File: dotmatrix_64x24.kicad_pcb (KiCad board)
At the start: 2 copper layers, 180 x 100 mm, 597 parts, among them CON1 BARREL_JACK, P1 CONN_01X09, P2 CONN_01X09, P3 CONN_01X04, P4 CONN_01X03, P5 USB_OTG, P6 CONN_01X03, Q1 NJL7302L-F3, Q2 Q_PNP_BEC 2SA1162, Q3 Q_NPN_BCE RN5006, SW1 SW_PUSH_SMALL_H, SW2 SW_PUSH_SMALL_H, SW3 SW_PUSH_SMALL_H, SW4 SW_PUSH_SMALL_H, SW5 SW_PUSH_SMALL_H, SW6 SW_PUSH_SMALL_H, SW7 SW_PUSH_SMALL_H, SW8 SW_PUSH_SMALL_H, U1 WROOM-02, U10 LED1642GW, U11 LED1642GW, U12 AE-BME280, U13 OKL-T/6-W5, U14 NJU7223, U15 DS1307, U16 CH340G, U17 OSRB38C9AA, U18 BME280, U2 74HC595-alt-vdd, U3 TD62783, U4 74HC595-alt-vdd, U5 TD62783, U6 LED1642GW, U7 74HC595-alt-vdd, U8 TD62783, U9 LED1642GW, X1 CRYSTAL_SMD, Y1 12MHz

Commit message: Various fix and improvements
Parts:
- added C35: 1u, Capacitors_SMD:C_0603_HandSoldering, F.Cu at (22.3, 108.3)
- added REF**: stitch-via-0.6mm, components:stitch-via-0.6mm, F.Cu at (68.4, 99.7)
- added REF**: stitch-via-0.6mm, components:stitch-via-0.6mm, F.Cu at (16.7, 103.5)
- added REF**: stitch-via-0.6mm, components:stitch-via-0.6mm, F.Cu at (20.4, 105.9)
- added REF**: stitch-via-0.6mm, components:stitch-via-0.6mm, F.Cu at (19.3, 105.1)
- added REF**: stitch-via-0.6mm, components:stitch-via-0.6mm, F.Cu at (137.9, 78.0)
- added REF**: stitch-via-0.6mm, components:stitch-via-0.6mm, F.Cu at (93.8, 84.6)
- added REF**: stitch-via-0.6mm, components:stitch-via-0.6mm, F.Cu at (101.5, 91.3)
- added REF**: stitch-via-0.6mm, components:stitch-via-0.6mm, F.Cu at (105.2, 91.1)
- added REF**: stitch-via-0.6mm, components:stitch-via-0.6mm, F.Cu at (105.4, 93.6)
- added REF**: stitch-via-0.6mm, components:stitch-via-0.6mm, F.Cu at (90.9, 88.5)
- added REF**: stitch-via-0.6mm, components:stitch-via-0.6mm, F.Cu at (102.9, 87.9)
- added REF**: stitch-via-0.6mm, components:stitch-via-0.6mm, F.Cu at (69.4, 102.4)
- added REF**: stitch-via-0.6mm, components:stitch-via-0.6mm, F.Cu at (110.8, 77.4)
- added REF**: stitch-via-0.6mm, components:stitch-via-0.6mm, F.Cu at (132.2, 95.4)
- added REF**: stitch-via-0.6mm, components:stitch-via-0.6mm, F.Cu at (134.0, 104.5)
- added REF**: stitch-via-0.6mm, components:stitch-via-0.6mm, F.Cu at (129.9, 105.6)
- added REF**: stitch-via-0.6mm, components:stitch-via-0.6mm, F.Cu at (131.7, 102.2)
- added REF**: stitch-via-0.6mm, components:stitch-via-0.6mm, F.Cu at (115.0, 96.2)
- added REF**: stitch-via-0.6mm, components:stitch-via-0.6mm, F.Cu at (107.6, 91.9)
- added REF**: stitch-via-0.6mm, components:stitch-via-0.6mm, F.Cu at (109.6, 97.8)
- added REF**: stitch-via-0.6mm, components:stitch-via-0.6mm, F.Cu at (104.7, 99.3)
- added REF**: stitch-via-0.6mm, components:stitch-via-0.6mm, F.Cu at (106.3, 104.0)
- added REF**: stitch-via-0.6mm, components:stitch-via-0.6mm, F.Cu at (66.9, 102.5)
- added REF**: stitch-via-0.6mm, components:stitch-via-0.6mm, F.Cu at (112.9, 104.7)
- added REF**: stitch-via-0.6mm, components:stitch-via-0.6mm, F.Cu at (61.6, 104.1)
- added REF**: stitch-via-0.6mm, components:stitch-via-0.6mm, F.Cu at (44.8, 101.6)
- added REF**: stitch-via-0.6mm, components:stitch-via-0.6mm, F.Cu at (20.7, 107.3)
- added REF**: stitch-via-0.6mm, components:stitch-via-0.6mm, F.Cu at (23.6, 109.4)
- added REF**: stitch-via-0.6mm, components:stitch-via-0.6mm, F.Cu at (22.4, 110.9)
- added REF**: stitch-via-0.6mm, components:stitch-via-0.6mm, F.Cu at (20.7, 109.1)
- moved REF** 4.28 mm to (15.4, 103.5)
- moved REF** 2.46 mm to (182.7, 105.3)
- moved REF** 2.22 mm to (84.5, 78.3)
- moved REF** 2.18 mm to (106.7, 94.7)
- moved REF** 2.00 mm to (102.6, 100.4)
- moved REF** 1.65 mm to (57.5, 104.4)
- moved REF** 1.60 mm to (131.1, 78.1)
- moved REF** 1.16 mm to (20.1, 103.6)
- moved REF** 1.05 mm to (130.0, 95.4)
- moved JP7 0.66 mm to (183.8, 85.4)
- moved REF** 0.39 mm to (181.4, 86.8)
- moved REF** 0.23 mm to (109.8, 100.0)
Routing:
- net GND: track 1029.2 -> 1016.7 mm
- net VCC: track 570.9 -> 574.6 mm
- net /ESPVDD: track 210.1 -> 213.2 mm
- net Net-(JP7-Pad2): track 4.93 -> 6.00 mm

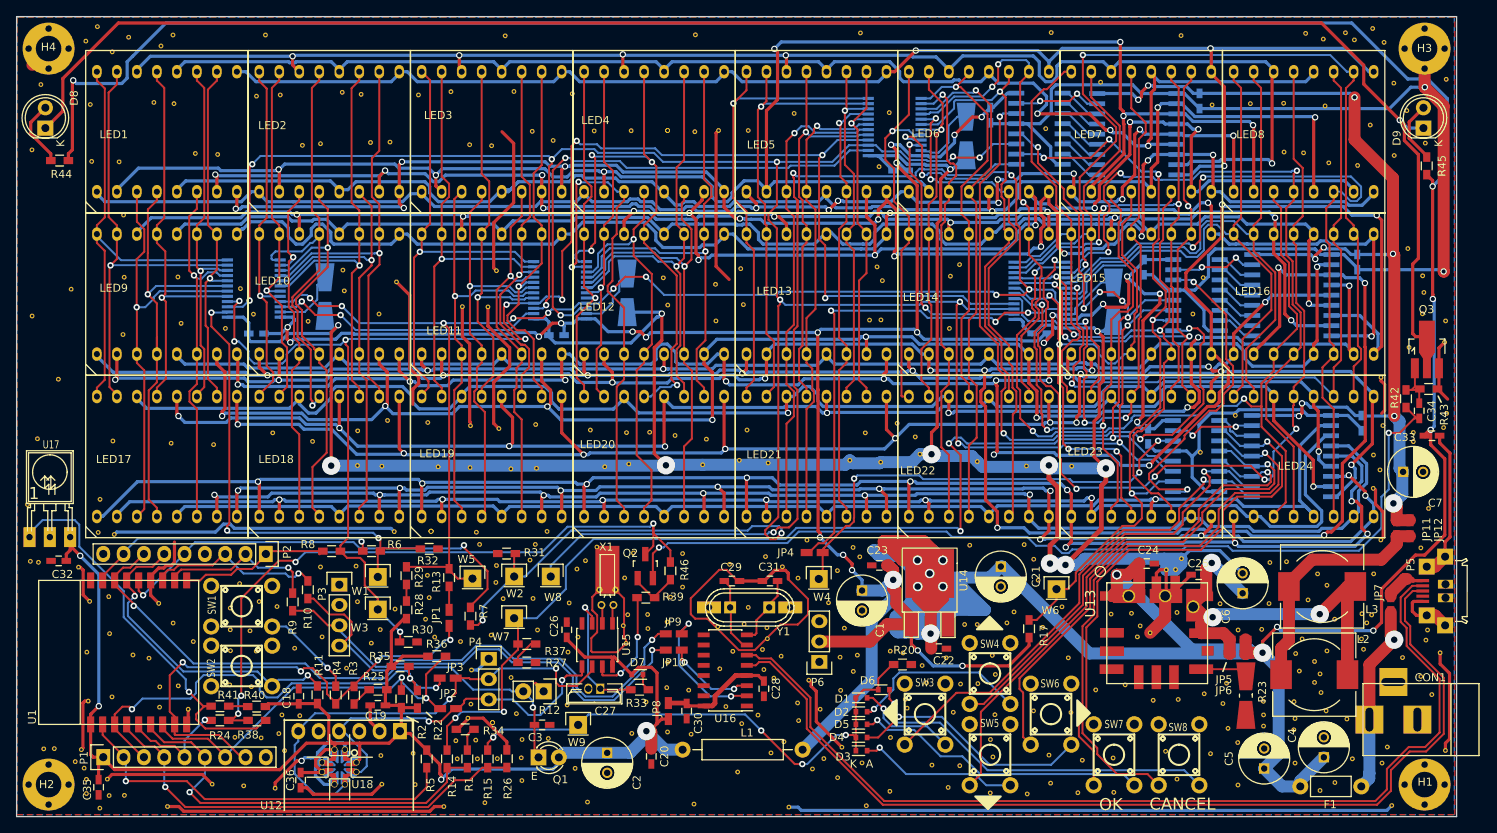
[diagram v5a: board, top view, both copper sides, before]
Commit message: Fixed current flow, cut antenna area of the PCB
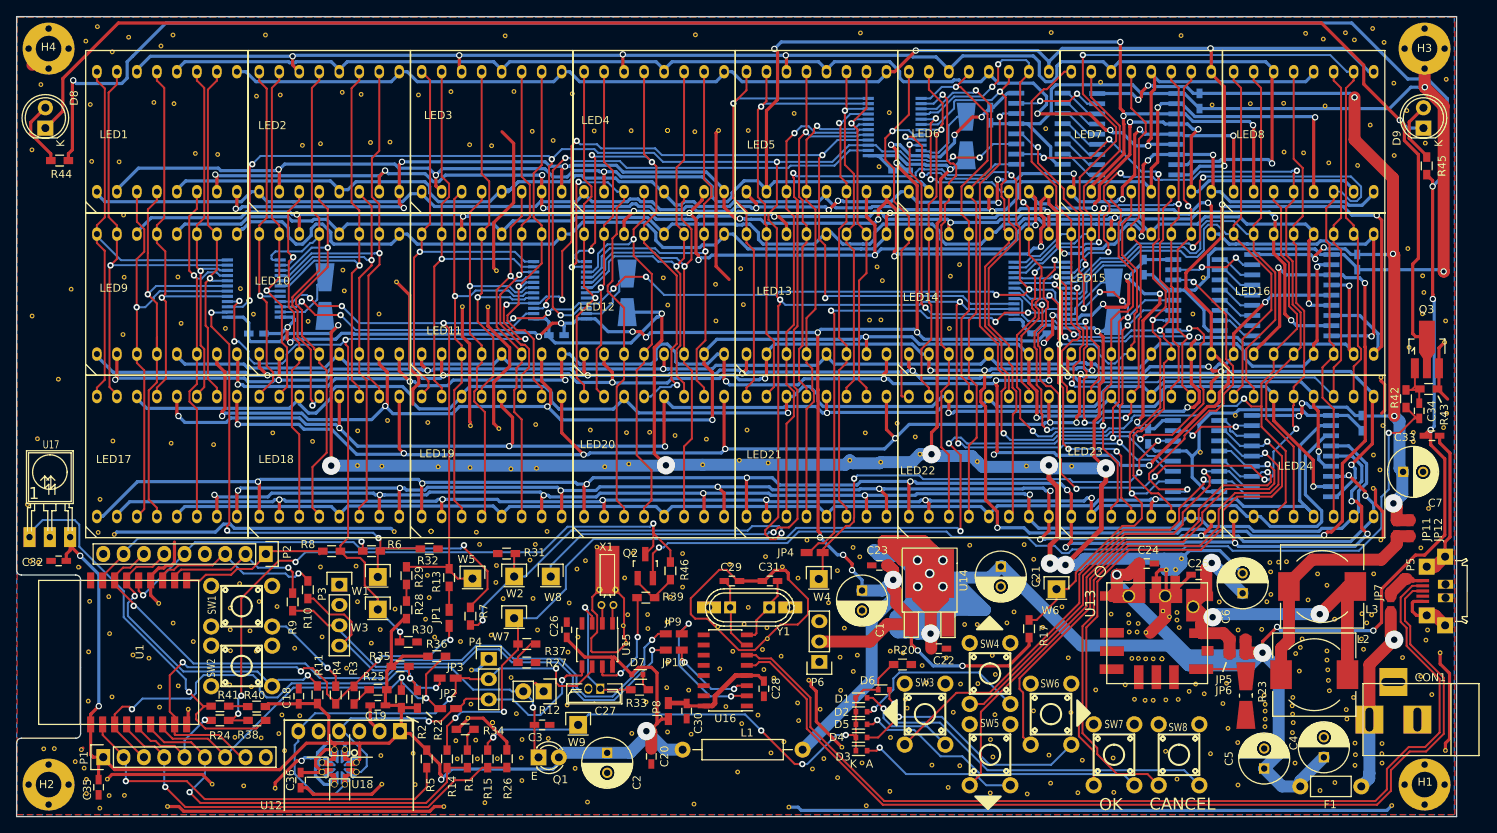
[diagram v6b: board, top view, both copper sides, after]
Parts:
- removed the REF** at (152.1, 89.5)
- added REF**: stitch-via-0.6mm, components:stitch-via-0.6mm, F.Cu at (168.8, 84.2)
- added REF**: stitch-via-0.6mm, components:stitch-via-0.6mm, F.Cu at (171.5, 101.5)
- added REF**: stitch-via-0.6mm, components:stitch-via-0.6mm, F.Cu at (171.4, 98.1)
- added REF**: stitch-via-0.6mm, components:stitch-via-0.6mm, F.Cu at (168.1, 98.0)
- added REF**: stitch-via-0.6mm, components:stitch-via-0.6mm, F.Cu at (159.4, 95.4)
- added REF**: stitch-via-0.6mm, components:stitch-via-0.6mm, F.Cu at (158.6, 96.3)
- added REF**: stitch-via-0.6mm, components:stitch-via-0.6mm, F.Cu at (155.7, 97.4)
- added REF**: stitch-via-0.6mm, components:stitch-via-0.6mm, F.Cu at (151.7, 97.3)
- added REF**: stitch-via-0.6mm, components:stitch-via-0.6mm, F.Cu at (153.1, 97.5)
- added REF**: stitch-via-0.6mm, components:stitch-via-0.6mm, F.Cu at (155.3, 86.3)
- added REF**: stitch-via-0.6mm, components:stitch-via-0.6mm, F.Cu at (156.1, 87.0)
- added REF**: stitch-via-0.6mm, components:stitch-via-0.6mm, F.Cu at (169.7, 80.2)
- added REF**: stitch-via-0.6mm, components:stitch-via-0.6mm, F.Cu at (157.3, 88.4)
- added REF**: stitch-via-0.6mm, components:stitch-via-0.6mm, F.Cu at (157.0, 87.4)
- added REF** (x2): stitch-via-0.6mm, components:stitch-via-0.6mm, F.Cu at (155.2, 92.3)
- added REF**: stitch-via-0.6mm, components:stitch-via-0.6mm, F.Cu at (154.1, 92.3)
- added REF**: stitch-via-0.6mm, components:stitch-via-0.6mm, F.Cu at (153.1, 92.3)
- added REF**: stitch-via-0.6mm, components:stitch-via-0.6mm, F.Cu at (152.2, 92.2)
- added REF**: stitch-via-0.6mm, components:stitch-via-0.6mm, F.Cu at (151.4, 92.2)
- added REF**: stitch-via-0.6mm, components:stitch-via-0.6mm, F.Cu at (151.0, 87.8)
- added REF**: stitch-via-0.6mm, components:stitch-via-0.6mm, F.Cu at (151.1, 88.9)
- added REF**: stitch-via-0.6mm, components:stitch-via-0.6mm, F.Cu at (168.8, 81.4)
- added REF**: stitch-via-0.6mm, components:stitch-via-0.6mm, F.Cu at (152.1, 88.9)
- added REF**: stitch-via-0.6mm, components:stitch-via-0.6mm, F.Cu at (179.3, 105.6)
- added REF**: stitch-via-0.6mm, components:stitch-via-0.6mm, F.Cu at (179.3, 104.3)
- added REF**: stitch-via-0.6mm, components:stitch-via-0.6mm, F.Cu at (182.7, 104.1)
- added REF**: stitch-via-0.6mm, components:stitch-via-0.6mm, F.Cu at (178.2, 98.6)
- added REF**: stitch-via-0.6mm, components:stitch-via-0.6mm, F.Cu at (172.5, 90.9)
- added REF**: stitch-via-0.6mm, components:stitch-via-0.6mm, F.Cu at (168.0, 100.8)
- moved REF** 3.82 mm to (179.1, 97.1)
- moved REF** 1.98 mm to (179.3, 102.8)
- moved REF** 1.75 mm to (176.0, 95.0)
- moved REF** 1.56 mm to (175.8, 92.4)
- moved REF** 1.09 mm to (175.9, 93.6)
- moved REF** 1.07 mm to (176.1, 96.3)
- moved REF** 0.89 mm to (171.6, 100.3)
- moved REF** 0.89 mm to (168.1, 99.8)
- moved REF** 0.79 mm to (182.7, 102.9)
- moved REF** 0.74 mm to (167.9, 96.9)
- moved REF** 0.64 mm to (171.5, 99.2)
- moved REF** 0.55 mm to (171.5, 97.1)
- moved REF** 0.54 mm to (153.2, 89.0)
- moved REF** 0.52 mm to (168.1, 98.8)
- moved REF** 0.40 mm to (152.2, 87.9)
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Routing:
- net GND: track 1016.7 -> 1005.6 mm
- net VCC: track 574.6 -> 569.9 mm
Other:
- outline, holes or cut-outs redrawn

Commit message: Various fixes, notably removing front coppor pour under Murata DC-DC converter
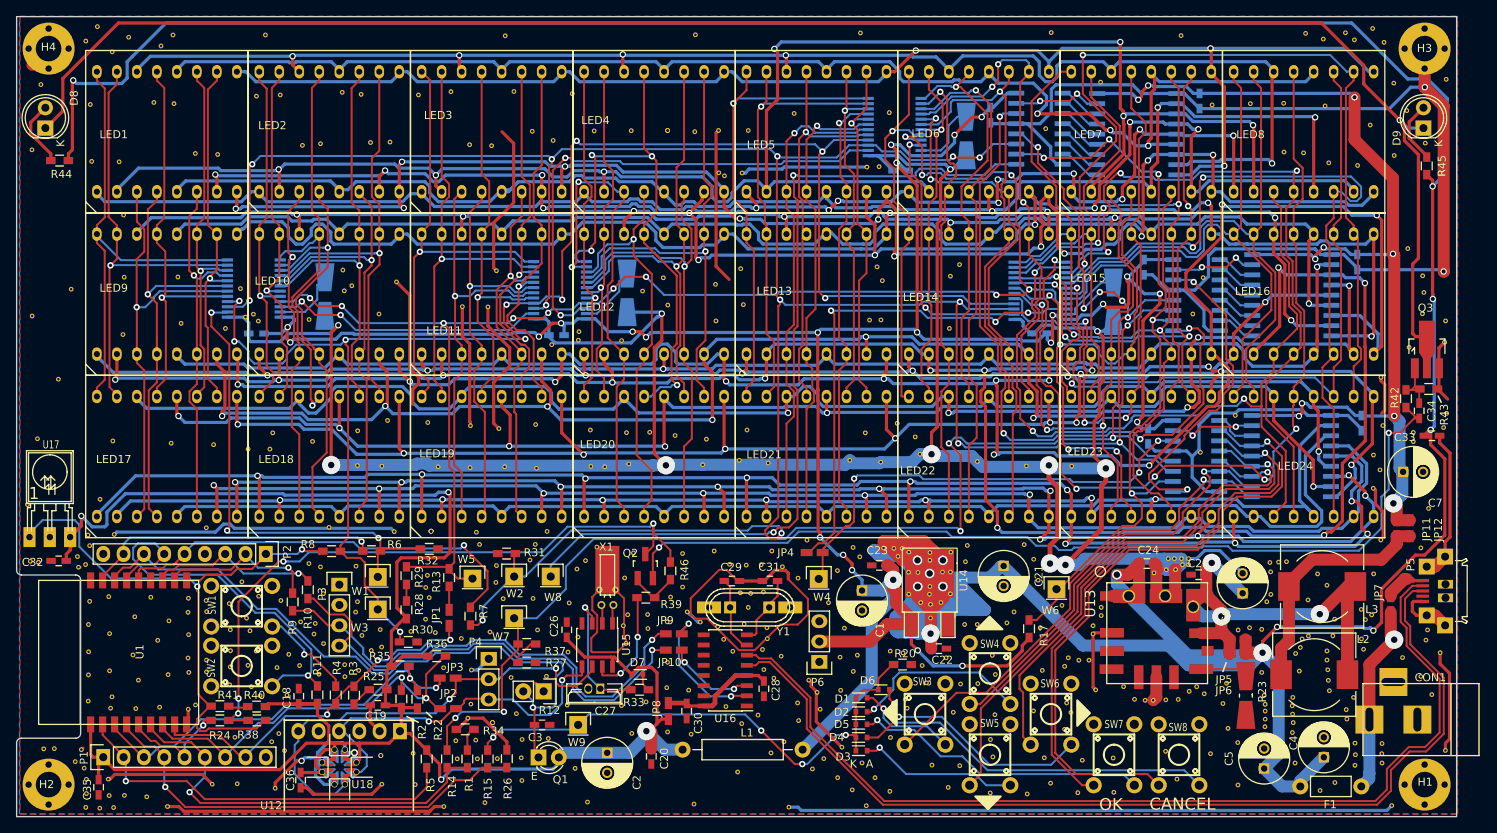
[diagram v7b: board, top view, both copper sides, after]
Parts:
- removed the REF** at (152.2, 87.9)
- removed the REF** at (162.3, 85.2)
- removed the REF** at (40.4, 108.2)
- removed the REF** at (155.3, 86.3)
- removed the REF** at (44.6, 85.8)
- removed the REF** at (156.1, 87.0)
- removed the REF** at (157.3, 88.4)
- removed the REF** at (157.0, 87.4)
- removed the REF** at (155.2, 92.3) (x2)
- removed the REF** at (154.1, 92.3)
- removed the REF** at (153.1, 92.3)
- removed the REF** at (152.2, 92.2)
- removed the REF** at (29.8, 85.3)
- removed the REF** at (42.6, 102.2)
- removed the REF** at (151.4, 92.2)
- removed the REF** at (151.0, 87.8)
- removed the REF** at (151.1, 88.9)
- removed the REF** at (152.1, 88.9)
- removed the REF** at (153.2, 89.0)
- removed the REF** at (148.8, 86.7)
- removed the REF** at (42.3, 85.1)
- removed the REF** at (47.4, 99.4)
- removed the REF** at (45.2, 99.3)
- removed the REF** at (151.0, 86.7)
- removed the REF** at (157.0, 86.5)
- removed the REF** at (38.7, 85.9)
- removed the REF** at (59.3, 86.1)
- added REF**: stitch-via-0.6mm, components:stitch-via-0.6mm, F.Cu at (106.4, 78.8)
- added REF**: stitch-via-0.6mm, components:stitch-via-0.6mm, F.Cu at (147.6, 85.9)
- added REF**: stitch-via-0.6mm, components:stitch-via-0.6mm, F.Cu at (49.2, 89.2)
- added REF**: stitch-via-0.6mm, components:stitch-via-0.6mm, F.Cu at (42.3, 84.5)
- added REF**: stitch-via-0.6mm, components:stitch-via-0.6mm, F.Cu at (40.7, 87.2)
- added REF**: stitch-via-0.6mm, components:stitch-via-0.6mm, F.Cu at (38.6, 85.4)
- added REF**: stitch-via-0.6mm, components:stitch-via-0.6mm, F.Cu at (40.9, 93.1)
- added REF**: stitch-via-0.6mm, components:stitch-via-0.6mm, F.Cu at (38.7, 93.3)
- added REF**: stitch-via-0.6mm, components:stitch-via-0.6mm, F.Cu at (44.6, 93.4)
- added REF**: stitch-via-0.6mm, components:stitch-via-0.6mm, F.Cu at (47.4, 93.1)
- added REF**: stitch-via-0.6mm, components:stitch-via-0.6mm, F.Cu at (43.9, 102.6)
- added REF**: stitch-via-0.6mm, components:stitch-via-0.6mm, F.Cu at (23.6, 93.8)
- added REF**: stitch-via-0.6mm, components:stitch-via-0.6mm, F.Cu at (144.8, 92.5)
- added REF**: stitch-via-0.6mm, components:stitch-via-0.6mm, F.Cu at (30.9, 94.3)
- added REF**: stitch-via-0.6mm, components:stitch-via-0.6mm, F.Cu at (27.2, 94.9)
- added REF**: stitch-via-0.6mm, components:stitch-via-0.6mm, F.Cu at (29.6, 90.0)
- added REF**: stitch-via-0.6mm, components:stitch-via-0.6mm, F.Cu at (31.0, 87.5)
- added REF**: stitch-via-0.6mm, components:stitch-via-0.6mm, F.Cu at (26.8, 87.0)
- added REF**: stitch-via-0.6mm, components:stitch-via-0.6mm, F.Cu at (28.8, 84.6)
- added REF**: stitch-via-0.6mm, components:stitch-via-0.6mm, F.Cu at (23.7, 98.5)
- added REF**: stitch-via-0.6mm, components:stitch-via-0.6mm, F.Cu at (34.4, 98.0)
- added REF**: stitch-via-0.6mm, components:stitch-via-0.6mm, F.Cu at (35.8, 86.4)
- added REF**: stitch-via-0.6mm, components:stitch-via-0.6mm, F.Cu at (35.7, 93.9)
- added REF**: stitch-via-0.6mm, components:stitch-via-0.6mm, F.Cu at (146.1, 92.5)
- added REF**: stitch-via-0.6mm, components:stitch-via-0.6mm, F.Cu at (35.7, 92.4)
- added REF**: stitch-via-0.6mm, components:stitch-via-0.6mm, F.Cu at (35.7, 85.0)
- added REF**: stitch-via-0.6mm, components:stitch-via-0.6mm, F.Cu at (143.0, 101.1)
- added REF**: stitch-via-0.6mm, components:stitch-via-0.6mm, F.Cu at (143.3, 97.8)
- added REF**: stitch-via-0.6mm, components:stitch-via-0.6mm, F.Cu at (146.6, 89.2)
- added REF**: stitch-via-0.6mm, components:stitch-via-0.6mm, F.Cu at (143.0, 93.2)
- added REF**: stitch-via-0.6mm, components:stitch-via-0.6mm, F.Cu at (140.2, 93.7)
- added REF**: stitch-via-0.6mm, components:stitch-via-0.6mm, F.Cu at (154.2, 81.5)
- added REF**: stitch-via-0.6mm, components:stitch-via-0.6mm, F.Cu at (157.7, 80.5)
- added REF**: stitch-via-0.6mm, components:stitch-via-0.6mm, F.Cu at (99.2, 78.8)
- added REF**: stitch-via-0.6mm, components:stitch-via-0.6mm, F.Cu at (158.5, 80.5)
- added REF**: stitch-via-0.6mm, components:stitch-via-0.6mm, F.Cu at (158.5, 79.8)
- added REF**: stitch-via-0.6mm, components:stitch-via-0.6mm, F.Cu at (156.7, 79.8)
- added REF**: stitch-via-0.6mm, components:stitch-via-0.6mm, F.Cu at (156.0, 79.8)
- added REF**: stitch-via-0.6mm, components:stitch-via-0.6mm, F.Cu at (130.6, 80.1)
- added REF**: stitch-via-0.6mm, components:stitch-via-0.6mm, F.Cu at (126.2, 87.2)
- added REF**: stitch-via-0.6mm, components:stitch-via-0.6mm, F.Cu at (126.2, 85.5)
- added REF**: stitch-via-0.6mm, components:stitch-via-0.6mm, F.Cu at (127.5, 85.2)
- added REF**: stitch-via-0.6mm, components:stitch-via-0.6mm, F.Cu at (125.0, 85.2)
- added REF**: stitch-via-0.6mm, components:stitch-via-0.6mm, F.Cu at (122.7, 78.5)
- added REF**: stitch-via-0.6mm, components:stitch-via-0.6mm, F.Cu at (49.8, 94.2)
- added REF**: stitch-via-0.6mm, components:stitch-via-0.6mm, F.Cu at (122.2, 79.5)
- added REF**: stitch-via-0.6mm, components:stitch-via-0.6mm, F.Cu at (121.7, 78.5)
- added REF**: stitch-via-0.6mm, components:stitch-via-0.6mm, F.Cu at (120.4, 78.4)
- added REF**: stitch-via-0.6mm, components:stitch-via-0.6mm, F.Cu at (126.1, 84.2)
- added REF**: stitch-via-0.6mm, components:stitch-via-0.6mm, F.Cu at (126.2, 79.0)
- added REF**: stitch-via-0.6mm, components:stitch-via-0.6mm, F.Cu at (128.7, 81.4)
- added REF**: stitch-via-0.6mm, components:stitch-via-0.6mm, F.Cu at (123.5, 81.5)
- added REF**: stitch-via-0.6mm, components:stitch-via-0.6mm, F.Cu at (123.5, 84.2)
- added REF**: stitch-via-0.6mm, components:stitch-via-0.6mm, F.Cu at (128.7, 84.2)
- added REF**: stitch-via-0.6mm, components:stitch-via-0.6mm, F.Cu at (128.8, 78.9)
- added REF**: stitch-via-0.6mm, components:stitch-via-0.6mm, F.Cu at (166.1, 88.4)
- added REF**: stitch-via-0.6mm, components:stitch-via-0.6mm, F.Cu at (123.5, 78.9)
- added REF**: stitch-via-0.6mm, components:stitch-via-0.6mm, F.Cu at (126.2, 83.2)
- added REF**: stitch-via-0.6mm, components:stitch-via-0.6mm, F.Cu at (127.7, 81.4)
- added REF**: stitch-via-0.6mm, components:stitch-via-0.6mm, F.Cu at (124.7, 81.5)
- added REF**: stitch-via-0.6mm, components:stitch-via-0.6mm, F.Cu at (126.2, 80.0)
- added REF**: stitch-via-0.6mm, components:stitch-via-0.6mm, F.Cu at (100.5, 31.9)
- added REF**: stitch-via-0.6mm, components:stitch-via-0.6mm, F.Cu at (99.8, 31.5)
- added REF**: stitch-via-0.6mm, components:stitch-via-0.6mm, F.Cu at (102.7, 31.5)
- added REF**: stitch-via-0.6mm, components:stitch-via-0.6mm, F.Cu at (118.3, 30.8)
- added REF**: stitch-via-0.6mm, components:stitch-via-0.6mm, F.Cu at (83.8, 68.2)
- added REF**: stitch-via-0.6mm, components:stitch-via-0.6mm, F.Cu at (167.6, 94.0)
- added REF**: stitch-via-0.6mm, components:stitch-via-0.6mm, F.Cu at (78.9, 53.0)
- added REF**: stitch-via-0.6mm, components:stitch-via-0.6mm, F.Cu at (82.2, 52.5)
- added REF**: stitch-via-0.6mm, components:stitch-via-0.6mm, F.Cu at (82.3, 51.4)
- added REF**: stitch-via-0.6mm, components:stitch-via-0.6mm, F.Cu at (42.2, 50.1)
- added REF**: stitch-via-0.6mm, components:stitch-via-0.6mm, F.Cu at (40.6, 49.6)
- added REF**: stitch-via-0.6mm, components:stitch-via-0.6mm, F.Cu at (43.7, 66.1)
- added REF**: stitch-via-0.6mm, components:stitch-via-0.6mm, F.Cu at (40.9, 66.1)
- added REF**: stitch-via-0.6mm, components:stitch-via-0.6mm, F.Cu at (53.9, 45.6)
- added REF**: stitch-via-0.6mm, components:stitch-via-0.6mm, F.Cu at (87.6, 52.5)
- added REF**: stitch-via-0.6mm, components:stitch-via-0.6mm, F.Cu at (90.2, 46.3)
- added REF**: stitch-via-0.6mm, components:stitch-via-0.6mm, F.Cu at (173.5, 89.4)
- added REF**: stitch-via-0.6mm, components:stitch-via-0.6mm, F.Cu at (35.7, 75.9)
- added REF**: stitch-via-0.6mm, components:stitch-via-0.6mm, F.Cu at (61.3, 88.8)
- added REF**: stitch-via-0.6mm, components:stitch-via-0.6mm, F.Cu at (78.2, 94.5)
- added REF**: stitch-via-0.6mm, components:stitch-via-0.6mm, F.Cu at (65.4, 93.4)
- added REF**: stitch-via-0.6mm, components:stitch-via-0.6mm, F.Cu at (42.4, 96.9)
- added REF**: stitch-via-0.6mm, components:stitch-via-0.6mm, F.Cu at (45.8, 96.8)
- added REF**: stitch-via-0.6mm, components:stitch-via-0.6mm, F.Cu at (53.0, 94.5)
- added REF**: stitch-via-0.6mm, components:stitch-via-0.6mm, F.Cu at (112.1, 96.5)
- added REF**: stitch-via-0.6mm, components:stitch-via-0.6mm, F.Cu at (116.5, 108.7)
- added REF**: stitch-via-0.6mm, components:stitch-via-0.6mm, F.Cu at (119.3, 107.1)
- added REF**: stitch-via-0.6mm, components:stitch-via-0.6mm, F.Cu at (176.5, 89.4)
- added REF**: stitch-via-0.6mm, components:stitch-via-0.6mm, F.Cu at (97.5, 87.7)
- added REF**: stitch-via-0.6mm, components:stitch-via-0.6mm, F.Cu at (95.8, 86.4)
- added REF**: stitch-via-0.6mm, components:stitch-via-0.6mm, F.Cu at (100.4, 89.8)
- added REF**: stitch-via-0.6mm, components:stitch-via-0.6mm, F.Cu at (105.4, 83.9)
- added REF**: stitch-via-0.6mm, components:stitch-via-0.6mm, F.Cu at (102.5, 84.0)
- added REF**: stitch-via-0.6mm, components:stitch-via-0.6mm, F.Cu at (103.8, 84.1)
- added REF**: stitch-via-0.6mm, components:stitch-via-0.6mm, F.Cu at (103.2, 80.6)
- added REF**: stitch-via-0.6mm, components:stitch-via-0.6mm, F.Cu at (87.6, 98.1)
- added REF**: stitch-via-0.6mm, components:stitch-via-0.6mm, F.Cu at (21.0, 88.0)
- added REF**: stitch-via-0.6mm, components:stitch-via-0.6mm, F.Cu at (21.0, 94.3)
- added REF**: stitch-via-0.6mm, components:stitch-via-0.6mm, F.Cu at (146.6, 88.1)
- added REF**: stitch-via-0.6mm, components:stitch-via-0.6mm, F.Cu at (26.9, 98.5)
- added REF**: stitch-via-0.6mm, components:stitch-via-0.6mm, F.Cu at (24.1, 110.9)
- added REF**: stitch-via-0.6mm, components:stitch-via-0.6mm, F.Cu at (20.7, 110.8)
- added REF**: stitch-via-0.6mm, components:stitch-via-0.6mm, F.Cu at (39.6, 107.9)
- added REF**: stitch-via-0.6mm, components:stitch-via-0.6mm, F.Cu at (28.3, 109.5)
- added REF**: stitch-via-0.6mm, components:stitch-via-0.6mm, F.Cu at (51.1, 75.8)
- added REF**: stitch-via-0.6mm, components:stitch-via-0.6mm, F.Cu at (20.6, 80.5)
- added REF**: stitch-via-0.6mm, components:stitch-via-0.6mm, F.Cu at (19.6, 79.5)
- added REF**: stitch-via-0.6mm, components:stitch-via-0.6mm, F.Cu at (21.1, 78.1)
- added REF**: stitch-via-0.6mm, components:stitch-via-0.6mm, F.Cu at (57.5, 104.4)
- added REF**: stitch-via-0.6mm, components:stitch-via-0.6mm, F.Cu at (147.6, 86.9)
- added REF**: stitch-via-0.6mm, components:stitch-via-0.6mm, F.Cu at (63.1, 83.4)
- added REF**: stitch-via-0.6mm, components:stitch-via-0.6mm, F.Cu at (54.4, 86.4)
- added REF**: stitch-via-0.6mm, components:stitch-via-0.6mm, F.Cu at (57.6, 90.8)
- added REF**: stitch-via-0.6mm, components:stitch-via-0.6mm, F.Cu at (55.2, 89.4)
- added REF**: stitch-via-0.6mm, components:stitch-via-0.6mm, F.Cu at (54.8, 93.7)
- added REF**: stitch-via-0.6mm, components:stitch-via-0.6mm, F.Cu at (48.5, 80.4)
- added REF**: stitch-via-0.6mm, components:stitch-via-0.6mm, F.Cu at (50.3, 84.1)
- added REF**: stitch-via-0.6mm, components:stitch-via-0.6mm, F.Cu at (45.0, 85.0)
- added REF**: stitch-via-0.6mm, components:stitch-via-0.6mm, F.Cu at (49.3, 87.9)
- added REF**: stitch-via-0.6mm, components:stitch-via-0.6mm, F.Cu at (47.5, 87.7)
- moved REF** 9.97 mm to (33.4, 86.5)
- moved REF** 5.44 mm to (33.5, 84.7)
- moved REF** 4.88 mm to (33.4, 92.2)
- moved REF** 2.41 mm to (33.5, 89.3)
- moved REF** 2.13 mm to (33.5, 94.0)
- moved REF** 1.31 mm to (20.9, 76.8)
- moved REF** 1.15 mm to (105.1, 80.5)
- moved REF** 1.06 mm to (46.0, 91.7)
- moved REF** 0.91 mm to (56.3, 91.2)
- moved REF** 0.86 mm to (50.4, 90.4)
- moved REF** 0.83 mm to (73.0, 68.3)
- moved REF** 0.67 mm to (140.5, 104.6)
- moved REF** 0.56 mm to (64.3, 89.0)
- moved REF** 0.54 mm to (180.1, 86.1)
- moved REF** 0.49 mm to (53.0, 93.0)
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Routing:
- net /ESPVDD: track 213.2 -> 264.2 mm
- net VCC: track 569.9 -> 589.4 mm
- net Net-(JP1-Pad1): track 62.2 -> 45.8 mm, vias 4 -> 3
- net GND: track 1005.6 -> 1021.5 mm
- net Net-(C3-Pad1): track 73.1 -> 84.0 mm, vias 2 -> 1
- net Net-(P2-Pad6): track 40.7 -> 50.3 mm, vias 2 -> 1
- net Net-(JP3-Pad1): track 59.2 -> 52.5 mm, vias 3 -> 2
- net /Sheet57A04605/SEL6: track 75.1 -> 80.6 mm
- net Net-(R38-Pad2): track 50.7 -> 56.1 mm
- net /Sheet57A04605/SEL5: track 67.9 -> 71.3 mm
- net /Sheet57A04605/r19: track 182.7 -> 185.2 mm
- net /Sheet57A04605/c9: track 55.2 -> 53.0 mm
- net /Sheet57A04605/r21: track 211.5 -> 213.6 mm
- net /Sheet57A04605/r22: track 176.1 -> 178.1 mm
- net Net-(P2-Pad5): track 56.2 -> 54.8 mm, vias 2 -> 1
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
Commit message: Various fixes
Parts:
- removed the REF** at (132.1, 67.6)
- removed the REF** at (166.2, 22.9)
- moved REF** 0.69 mm to (159.8, 65.8)
- moved REF** 0.32 mm to (39.0, 102.2)
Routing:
- net /Sheet57A04605/c61: track 95.8 -> 86.1 mm
- net /Sheet57A04605/SEL4: track 63.5 -> 57.2 mm
- net /Sheet57A04605/SEL5: track 71.3 -> 66.9 mm
- net /Sheet57A04605/r3: track 202.6 -> 198.6 mm
- net /Sheet57A04605/SEL6: track 80.6 -> 76.8 mm
- net /Sheet57A04605/c57: track 114.5 -> 111.2 mm
- net /Sheet57A04605/SEL3: track 70.1 -> 67.2 mm
- net /Sheet57A04605/c58: track 103.1 -> 101.9 mm
- net /Sheet57A04605/r9: track 185.2 -> 186.3 mm
- net /Sheet57A04605/r6: track 198.4 -> 199.4 mm
- net /Sheet57A04605/COLLATCH: track 203.4 -> 202.7 mm
- net /Sheet57A04605/c24: track 58.2 -> 57.5 mm
- net /Sheet57A04605/c44: track 62.7 -> 62.0 mm, vias 3 -> 2
- net Net-(P2-Pad1): track 19.5 -> 19.0 mm
- net /Sheet57A04605/c25: track 71.5 -> 70.9 mm
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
